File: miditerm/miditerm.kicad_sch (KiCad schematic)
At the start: 51 parts, among them J1 USB, J2 MIDI IN, J3 MIDI OUT, J4 GND, U1 USBLC6-2SC6, U2 FT231XS, U3 H11L1

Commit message: Cleanup
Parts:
- R11, R5, R6, R8: value 270R -> 220R
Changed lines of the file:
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@@
       (effects (font (size 1.27 1.27)) (justify left))
     )
-    (property "Value" "270R" (at 238.76 78.74 0)
+    (property "Value" "220R" (at 238.76 78.74 0)
       (effects (font (size 1.27 1.27)) (justify left))
     )
@@
       (effects (font (size 1.27 1.27)) (justify left))
     )
-    (property "Value" "270R" (at 228.6 78.74 0)
+    (property "Value" "220R" (at 228.6 78.74 0)
       (effects (font (size 1.27 1.27)) (justify left))
     )
@@
       (effects (font (size 1.27 1.27)) (justify left))
     )
-    (property "Value" "270R" (at 124.46 133.35 0)
+    (property "Value" "220R" (at 124.46 133.35 0)
       (effects (font (size 1.27 1.27)) (justify left))
     )
@@
       (effects (font (size 1.27 1.27)) (justify left))
     )
-    (property "Value" "270R" (at 39.37 34.29 0)
-      (effects (font (size 1.27 1.27)) (justify left))
-    )
+    (property "Value" "220R" (at 39.37 34.29 0)
+      (effects (font (size 1.27 1.27)) (justify left))
+    )

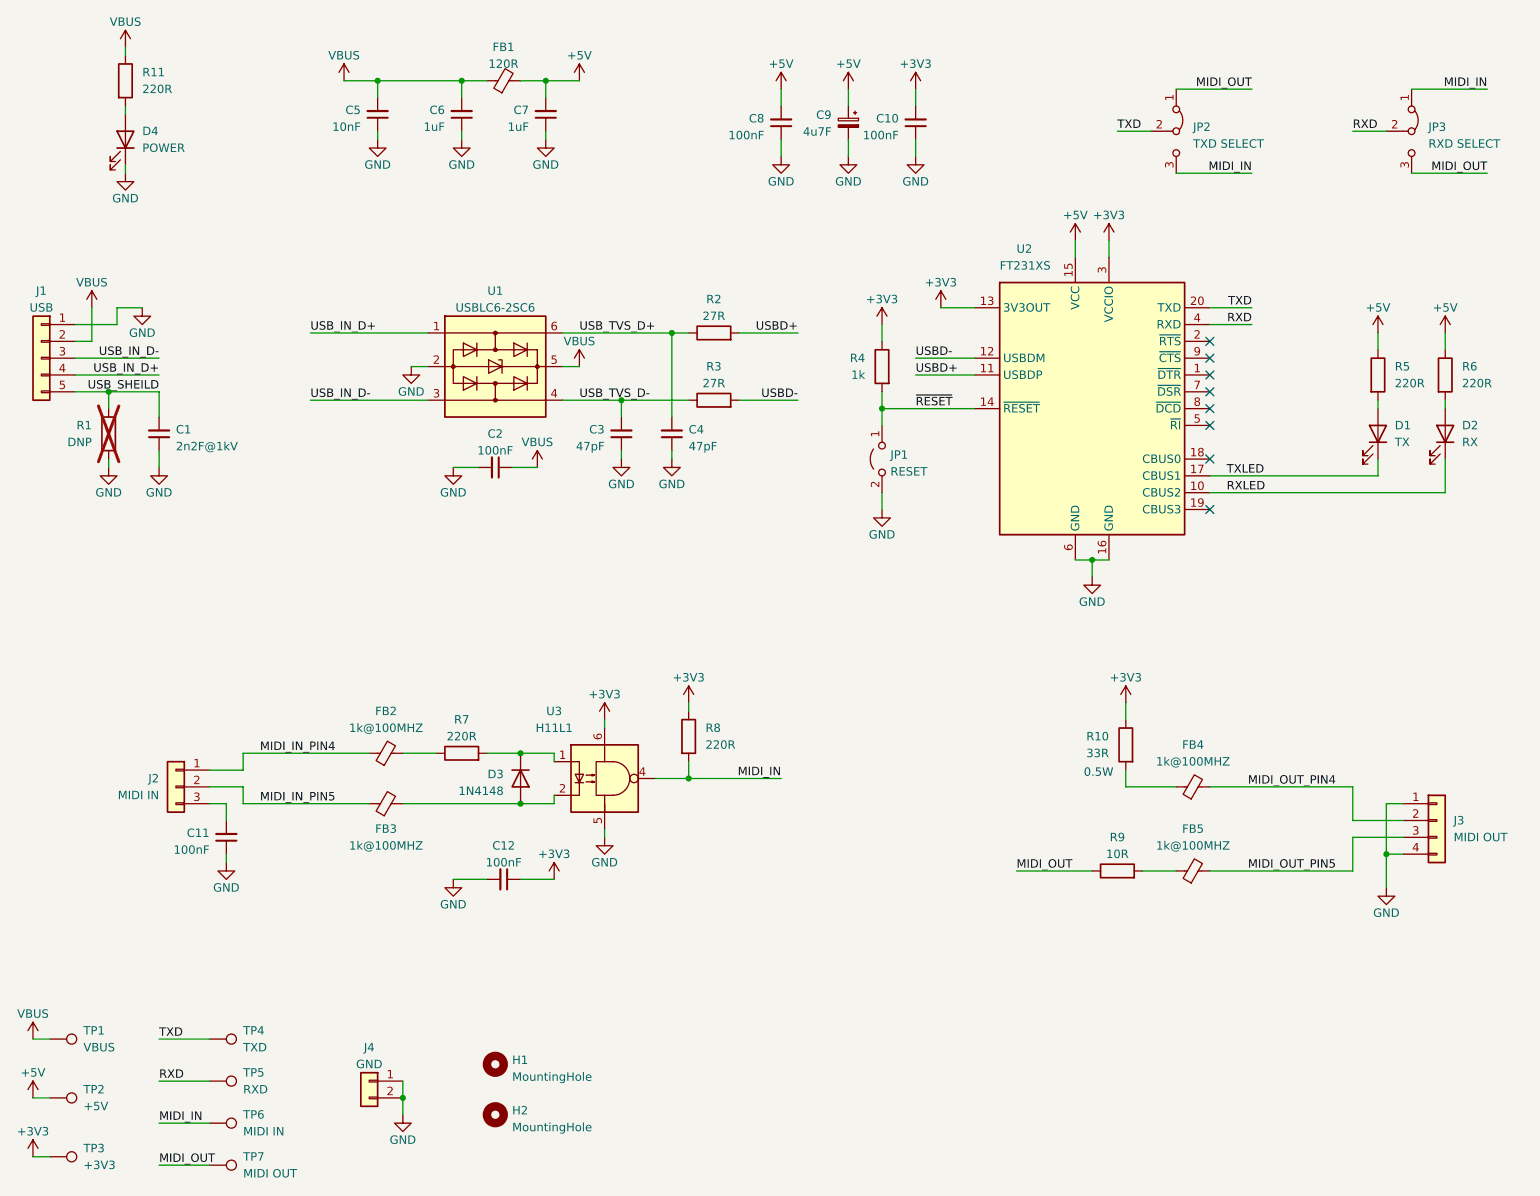
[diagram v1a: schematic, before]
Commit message: Update resistor values for LEDs
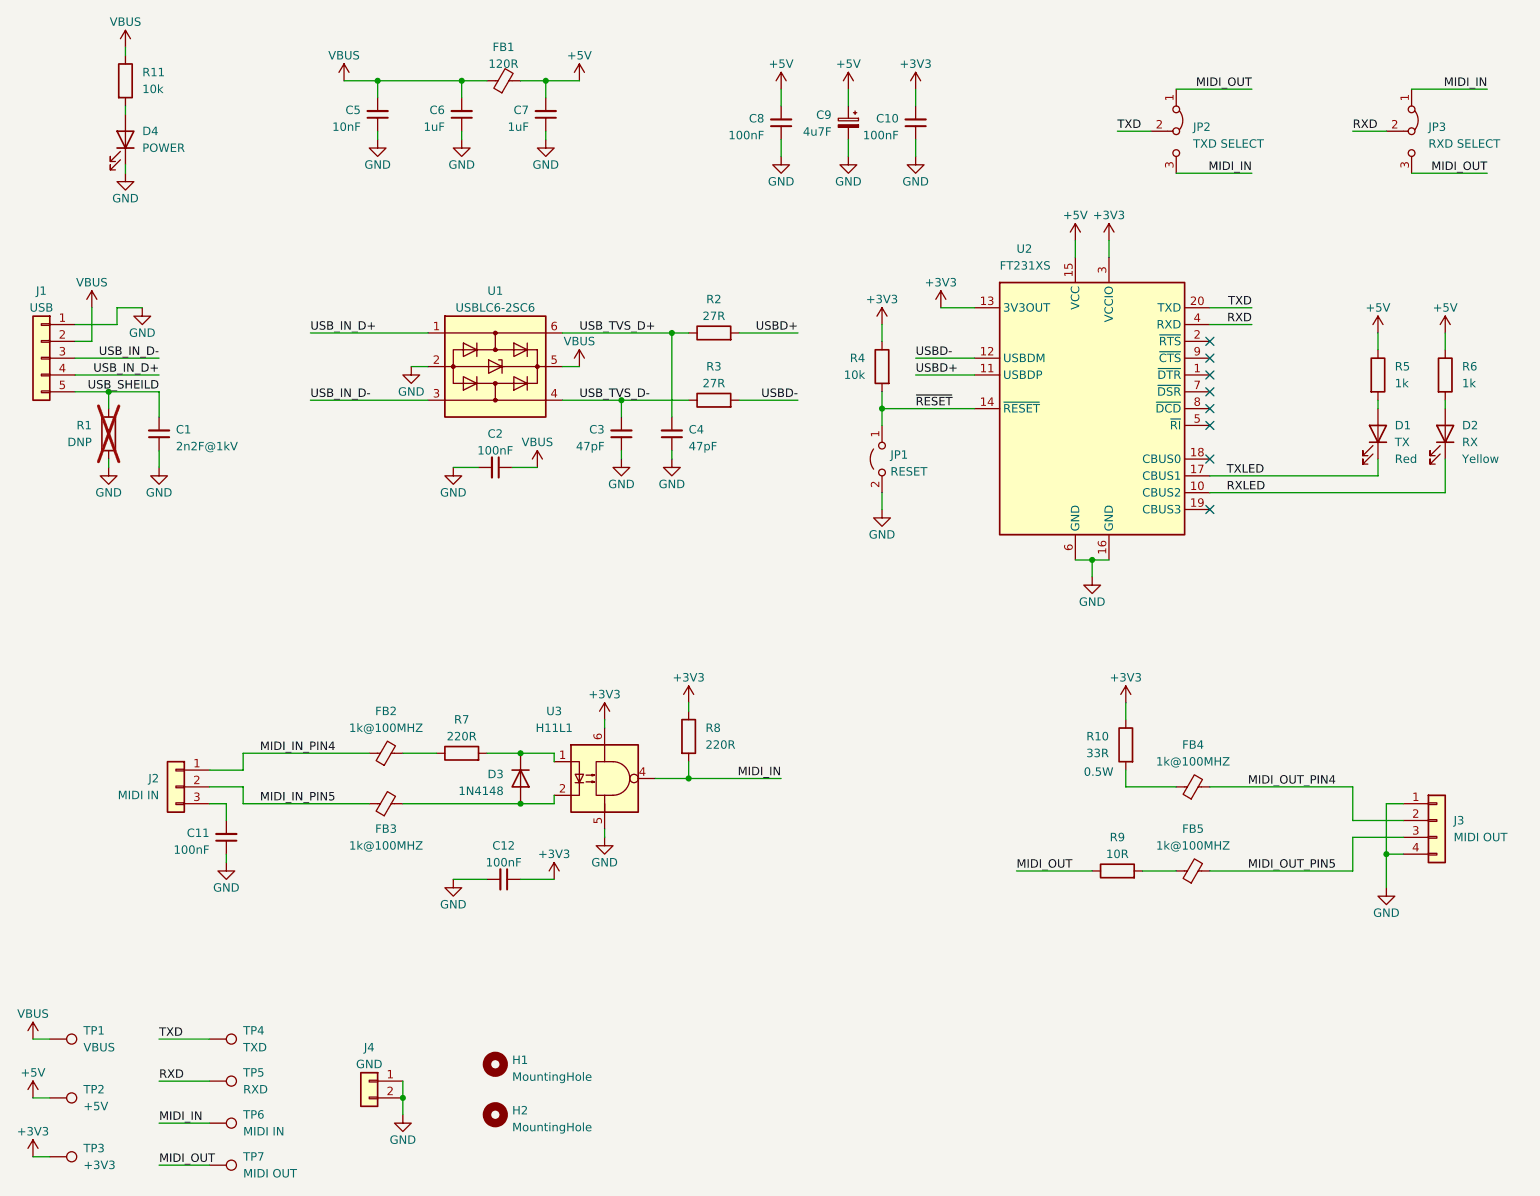
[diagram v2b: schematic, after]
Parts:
- D1: Color (none) -> Red
- D2: Color (none) -> Yellow
- R11: value 220R -> 10k
- R4: value 1k -> 10k
- R5, R6: value 220R -> 1k
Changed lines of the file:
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@@
       (effects (font (size 1.27 1.27)) (justify left))
     )
-    (property "Value" "220R" (at 238.76 78.74 0)
+    (property "Value" "1k" (at 238.76 78.74 0)
       (effects (font (size 1.27 1.27)) (justify left))
     )
@@
       (effects (font (size 1.27 1.27)) (justify left))
     )
-    (property "Value" "220R" (at 228.6 78.74 0)
+    (property "Value" "1k" (at 228.6 78.74 0)
       (effects (font (size 1.27 1.27)) (justify left))
     )
@@
       (effects (font (size 1.27 1.27)) (justify left))
     )
-    (property "Value" "1k" (at 148.59 77.47 0)
+    (property "Value" "10k" (at 148.59 77.47 0)
       (effects (font (size 1.27 1.27)) (justify left))
     )
@@
       (effects (font (size 1.27 1.27)) hide)
     )
+    (property "Color" "Red" (at 228.6 90.17 90)
+      (effects (font (size 1.27 1.27)) (justify left))
+    )
     (pin "1")
     (pin "2")
@@
       (effects (font (size 1.27 1.27)) (justify left))
     )
-    (property "Value" "220R" (at 39.37 34.29 0)
+    (property "Value" "10k" (at 39.37 34.29 0)
       (effects (font (size 1.27 1.27)) (justify left))
     )
@@
       (effects (font (size 1.27 1.27)) hide)
     )
-    (pin "1")
+    (property "Color" "Yellow" (at 238.76 90.17 90)
+      (effects (font (size 1.27 1.27)) (justify left))
+    )
+    (pin "1")
